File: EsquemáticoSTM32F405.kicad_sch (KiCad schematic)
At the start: 0 parts

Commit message: STM32 mapeo
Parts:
- added R7: 10k, Resistor_SMD:R_0402_1005Metric, symbol Device:R_Small
- added SW1: SW_SPDT, Button_Switch_SMD:SW_SPDT_PCM12, symbol Switch:SW_SPDT
- added U3: STM32F405RGTx, Package_QFP:LQFP-64_10x10mm_P0.5mm, symbol MCU_ST_STM32F4:STM32F405RGTx
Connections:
- new net: R7.1, SW1.2 (B)
- new net: U3.18 (VSS), U3.63 (VSS)
- new net +3.3V: SW1.1 (A)
- new net +3V3: U3.19 (VDD), U3.32 (VDD), U3.48 (VDD), U3.64 (VDD)
- new net +3VA3: U3.13 (VDDA)
- new net BOOT0: R7.2, U3.60 (BOOT0)
- new net GND: SW1.3 (C)

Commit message: STM32 actualización 25/03
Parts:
- removed U3: STM32F405RGTx, Package_QFP:LQFP-64_10x10mm_P0.5mm, symbol MCU_ST_STM32F4:STM32F405RGTx
- added C14, C15, C16, C17, C22: 100nF, easyeda2kicad:C0402, symbol CANSAT_STM32_symbols:TCC0402X7R104J500AT
- added C18: 10nF, Capacitor_SMD:C_0402_1005Metric, symbol Device:C
- added C19: 1uF, easyeda2kicad:C0402, symbol CANSAT_STM32_symbols:CGA0402X5R105K500GT
- added C20, C21: 2.2uF, easyeda2kicad:C0402, symbol CANSAT_STM32_symbols:GRM155Z71A225KE44D
- added L3: 1Kohm_100Mhz, easyeda2kicad:L0402, symbol CANSAT_STM32_symbols:BLM15HG102SN1D
- added U4: STM32F405RGT6, easyeda2kicad:LQFP-64_L10.0-W10.0-P0.50-LS12.0-BL, symbol CANSAT_STM32_symbols:STM32F405RGT6
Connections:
- net +3VA3: now also C18.1, C19.2, L3.2, U4.13 (VDDA)
- net BOOT0: now also U4.60 (BOOT0)
- net GND: now also C14.2, C15.2, C16.2, C17.2, C18.2, C19.1, C20.1, C21.1, C22.2, U4.12 (VSSA), U4.18 (VSS), U4.63 (VSS)
- new net: C21.2, U4.31 (VCAP_1)
- new net: C20.2, U4.47 (VCAP_2)
- new net +3VBAT: C22.1, U4.1 (VBAT)
- new net +3VDD3: C14.1, C15.1, C16.1, C17.1, L3.1, U4.19 (VDD), U4.32 (VDD), U4.48 (VDD), U4.64 (VDD)
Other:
- note added: "BUSES"
- note added: "POWER"
- moved on the sheet: R7, SW1

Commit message: AVANCE STM32
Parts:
- added X1: XTAL, easyeda2kicad:CRYSTAL-SMD_L3.2-W2.5_3225-8MHZ, symbol CANSAT_STM32_symbols:X22EL89COI-111YLC-8M
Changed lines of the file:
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@@
+	)
+	(symbol
+		(lib_id "CANSAT_STM32_symbols:X22EL89COI-111YLC-8M")
+		(at 285.75 190.5 0)
+		(unit 1)
+		(body_style 1)
+		(exclude_from_sim no)
+		(in_bom yes)
+		(on_board yes)
+		(in_pos_files yes)
+		(dnp no)
+		(fields_autoplaced yes)
+		(property "Reference" "X1"
+			(at 285.75 184.15 0)
+			(show_name no)
+			(do_not_autoplace no)
+			(effects
+				(font
+					(size 1.27 1.27)
+				)
+			)
+		)
+		(property "Value" "XTAL"
+			(at 285.75 186.69 0)
+			(show_name no)
+			(do_not_autoplace no)
+			(effects
+				(font
+					(size 1.27 1.27)
+				)
+			)
+		)
+		(property "Footprint" "easyeda2kicad:CRYSTAL-SMD_L3.2-W2.5_3225-8MHZ"
+			(at 285.75 198.12 0)
+			(hide yes)
+			(show_name no)
+			(do_not_autoplace no)
+			(effects
+				(font
+					(size 1.27 1.27)
+				)
+			)
+		)
+		(property "Datasheet" "https://www.lcsc.com/datasheet/C42448903.pdf"
+			(at 285.75 200.66 0)
+			(hide yes)
+			(show_name no)
+			(do_not_autoplace no)
+			(effects
+				(font
+					(size 1.27 1.27)
+				)
+			)
+		)
+		(property "Description" ""
+			(at 285.75 190.5 0)
+			(hide yes)
+			(show_name no)
+			(do_not_autoplace no)
+			(effects
+				(font
+					(size 1.27 1.27)
+				)
+			)
+		)
+		(property "Manufacturer" "YXC(扬兴晶振)"
+			(at 285.75 203.2 0)
+			(hide yes)
+			(show_name no)
+			(do_not_autoplace no)
+			(effects
+				(font
+					(size 1.27 1.27)
+				)
+			)
+		)
+		(property "MPN" "X22EL89COI-111YLC-8M"
+			(at 285.75 205.74 0)
+			(hide yes)
+			(show_name no)
+			(do_not_autoplace no)
+			(effects
+				(font
+					(size 1.27 1.27)
+				)
+			)
+		)
+		(property "LCSC Part" "C42448903"
+			(at 285.75 208.28 0)
+			(hide yes)
+			(show_name no)
+			(do_not_autoplace no)
+			(effects
+				(font
+					(size 1.27 1.27)
+				)
+			)
+		)
+		(pin "1"
+		)
+		(pin "2"
+		)
+		(instances
+			(project "ARLISS_STM32_2026"
+				(path "/9719ea46-14c4-4409-9c57-49dd5454c03f/55efcca8-1297-47b0-ad35-b3f1b6f19299"
+					(reference "X1")
+					(unit 1)
+				)
+			)
+		)
 	)
 	(symbol

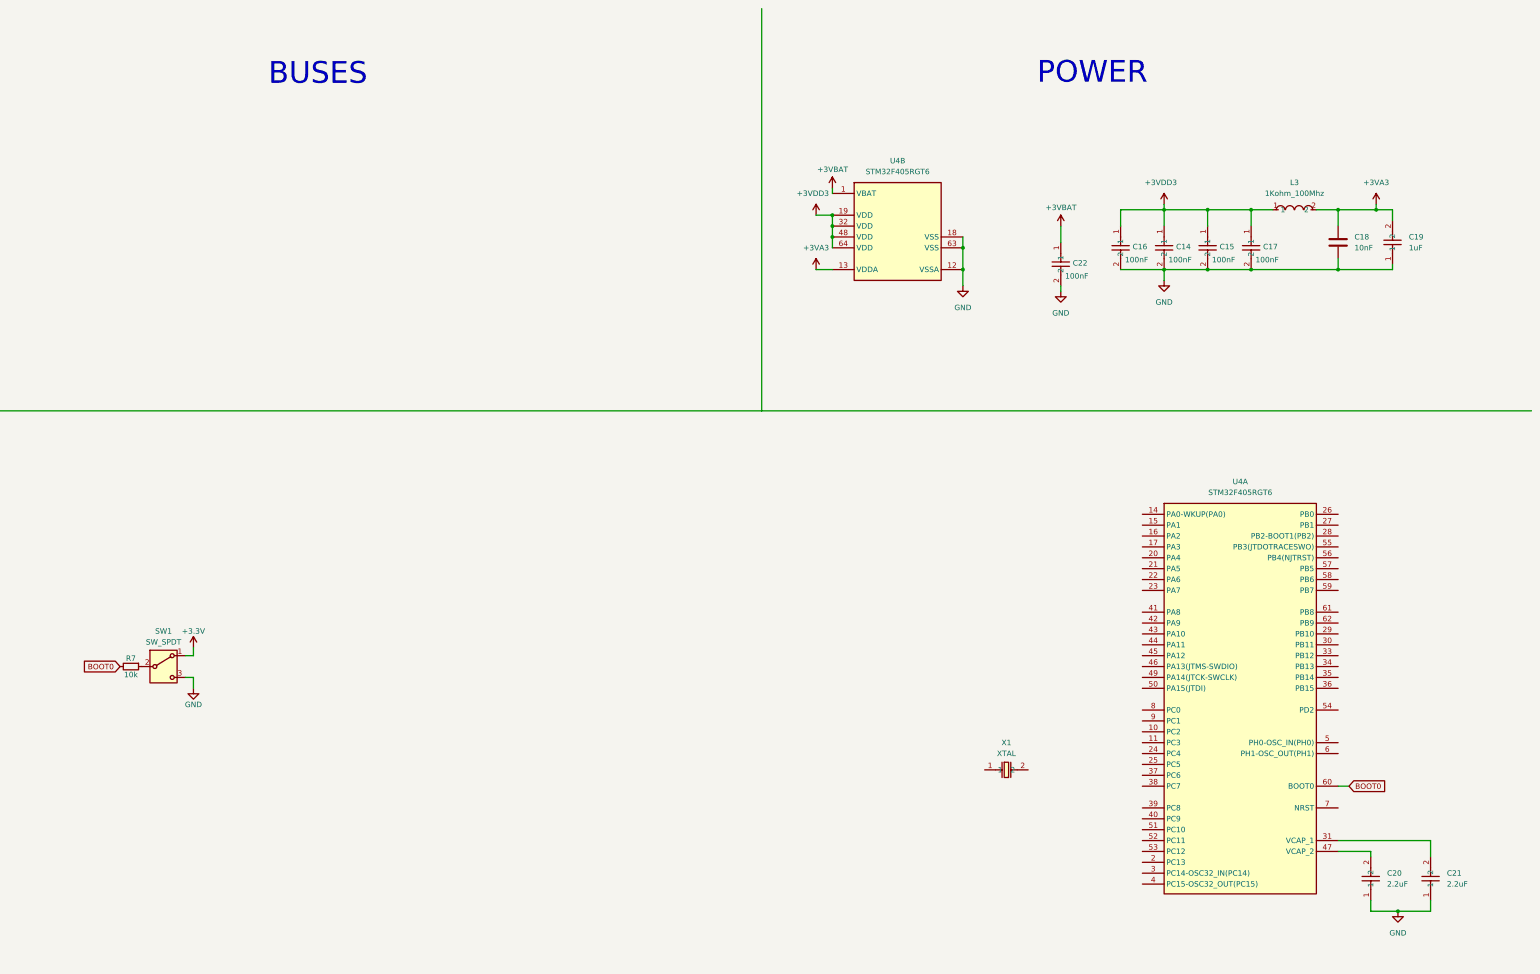
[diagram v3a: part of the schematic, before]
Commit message: Protocolos I2C/SPI
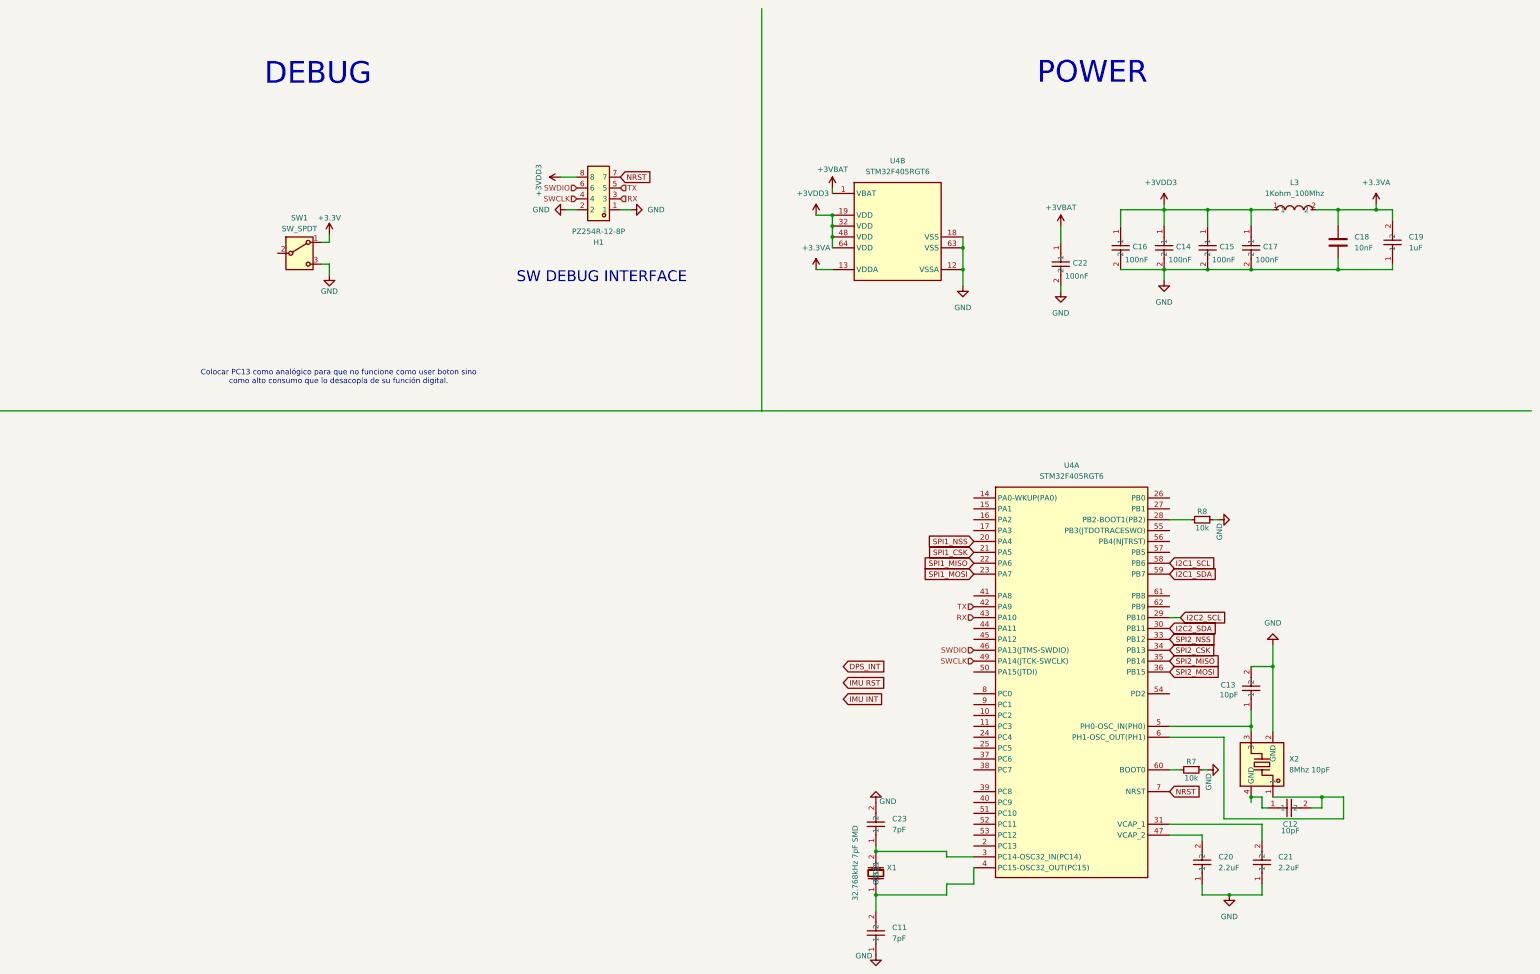
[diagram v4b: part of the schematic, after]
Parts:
- removed X1: XTAL, easyeda2kicad:CRYSTAL-SMD_L3.2-W2.5_3225-8MHZ, symbol CANSAT_STM32_symbols:X22EL89COI-111YLC-8M
- added C11, C23: 7pF, easyeda2kicad:C0402, symbol CANSAT_STM32_symbols:CC0402CRNPO9BN7R0
- added C12, C13: 10pF, easyeda2kicad:C0402, symbol CANSAT_STM32_symbols:CC0402FRNPO9BN100
- added H1: PZ254R-12-8P, easyeda2kicad:HDR-TH_8P-P2.54-H-M-R2-C4-S2.54, symbol CANSAT_STM32_symbols:PZ254R-12-8P
- added R8: 10k, Resistor_SMD:R_0402_1005Metric, symbol Device:R_Small
- added X1: 32.768kHz 7pF SMD, easyeda2kicad:FC-12M_L2.0-W1.2, symbol CANSAT_STM32_symbols:FC-12M32.768KHZ7PF20PPM
- added X2: 8Mhz 10pF, easyeda2kicad:CRYSTAL-SMD_4P-L3.2-W2.5-BL, symbol CANSAT_STM32_symbols:XTM32008000GT00351001
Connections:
- net +3VDD3: now also H1.8
- net GND: now also R7.1, C11.1, C13.2, C23.2, H1.1, H1.2, R8.1, X2.2 (GND)
- net at SW1.2 (B): no longer R7.1
- net SPI1_NSS: now reaches U4.20 (PA4)
- net SPI1_CSK: now reaches U4.21 (PA5)
- net SPI1_MISO: now reaches U4.22 (PA6)
- net SPI1_MOSI: now reaches U4.23 (PA7)
- net at U4.28 (PB2-BOOT1(PB2)): now also R8.2
- net I2C2_SCL: now reaches U4.29 (PB10)
- net at U4.3 (PC14-OSC32_IN(PC14)): now also C23.1, X1.2 (OSC2)
- net I2C2_SDA: now reaches U4.30 (PB11)
- net SPI2_NSS: now reaches U4.33 (PB12)
- net SPI2_CSK: now reaches U4.34 (PB13)
- net SPI2_MISO: now reaches U4.35 (PB14)
- net SPI2_MOSI: now reaches U4.36 (PB15)
- net at U4.4 (PC15-OSC32_OUT(PC15)): now also C11.2, X1.1 (OSC1)
- net TX: now reaches U4.42 (PA9)
- net TX: now also H1.5
- net RX: now reaches U4.43 (PA10)
- net RX: now also H1.3
- net SWDIO: now reaches U4.46 (PA13(JTMS-SWDIO))
- net SWDIO: now also H1.6
- net SWCLK: now reaches U4.49 (PA14(JTCK-SWCLK))
- net SWCLK: now also H1.4
- net at U4.5 (PH0-OSC_IN(PH0)): now also C13.1, X2.3
- net I2C1_SCL: now reaches U4.58 (PB6)
- net I2C1_SDA: now reaches U4.59 (PB7)
- net at U4.6 (PH1-OSC_OUT(PH1)): now also C12.2, X2.1
- net NRST: now reaches U4.7 (NRST)
- net NRST: now also H1.7
- net +3VA3 renamed +3.3VA
- net BOOT0: no longer names the net of R7.2, U4.60 (BOOT0)
- new net: C12.1, X2.4 (GND)
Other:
- note added: "Colocar PC13 como analógico para que no funcione como user boton sino como alto consumo que lo desacopla de su función digital."
- note added: "DEBUG"
- note added: "SW DEBUG INTERFACE"
- note removed: "BUSES"
- moved on the sheet: C20, C21, SW1, U4A

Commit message: ALIMENTACIÓN
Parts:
- removed SW1: SW_SPDT, Button_Switch_SMD:SW_SPDT_PCM12, symbol Switch:SW_SPDT
- added R10: 5.1K, symbol Device:R
- added U13: Green LED, easyeda2kicad:LED0603-FD, symbol CANSAT_STM32_symbols:YLED0603G
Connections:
- net +3VDD3 is gone; now on net +3.3V: C14.1, C15.1, C16.1, C17.1, H1.8, L3.1, U4.19 (VDD), U4.32 (VDD), U4.48 (VDD), U4.64 (VDD)
- net +3.3V: now also R10.1
- net GND: now also U13.2 (-); no longer C22.2
- net +3VBAT: no longer names the net of C22.1
- net +3VBAT: no longer U4.1 (VBAT)
- new net: R10.2, U13.1 (+)
- no-connect marks 0 -> 1
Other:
- moved on the sheet: C14, C15, C16, C17, C18, C19, L3, U4B

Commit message: Esquemático V1
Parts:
- added R11: RC0603FR-7W10KL, easyeda2kicad:R0603, symbol CANSAT_STM32_symbols:RC0603FR-7W10KL
- added SW3: XDTD-0304-215, easyeda2kicad:SW-SMD_L3.9-W3.0-P4.45, symbol CANSAT_STM32_symbols:XDTD-0304-215
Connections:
- net +3.3V: now also R11.2
- net ACEL_INT1: now also U4.27 (PB1)
- net ACEL_INT2: now also U4.26 (PB0)
- net ADC1: now also U4.15 (PA1)
- net ADC2: now also U4.9 (PC1)
- net ALERT1_INA226: now also U4.44 (PA11)
- net ALERT2_INA226: now also U4.45 (PA12)
- net DPS_INT: now also U4.57 (PB5)
- net GND: now also C22.2, SW3.2
- net IMU INT: now also U4.61 (PB8)
- net IMU RST: now also U4.62 (PB9)
- net M1_IN1: now also U4.37 (PC6)
- net M1_IN2: now also U4.38 (PC7)
- net M2_IN1: now also U4.39 (PC8)
- net M2_IN2: now also U4.40 (PC9)
- net NRST: now also C22.1, R11.1, SW3.1
- net PIN_MOSFET: now also U4.53 (PC12)
- net VREF/DAC1: now also U4.11 (PC3)
- net VREF/DAC2: now also U4.10 (PC2)
- net nSLEEP1: now also U4.25 (PC5)
- net nSLEEP2: now also U4.51 (PC10)
- net RADXA_RX: now reaches U4.16 (PA2)
- net RADXA_TX: now reaches U4.17 (PA3)
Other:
- moved on the sheet: C22, R8

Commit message: BECERRA
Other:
- note added: "DATASHEET"
- note added: "RESET INTERFACE"
- moved on the sheet: C11, C12, C13, C20, C21, C22, C23, H1, R11, R7, R8, SW3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
